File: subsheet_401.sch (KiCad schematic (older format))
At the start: 16 parts, among them U401 STE_GSTSHIFTER_PHY

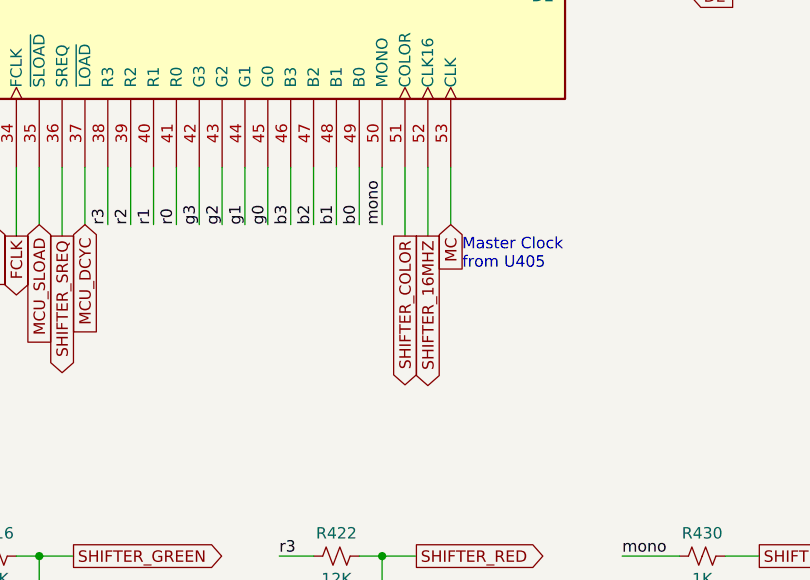
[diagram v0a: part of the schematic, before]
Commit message: Delete circuitry related to PAL/NTSC and modulator
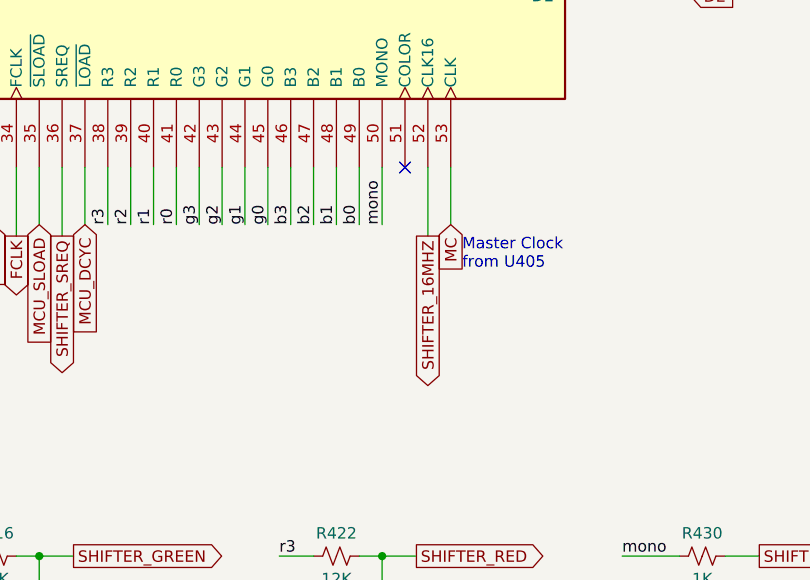
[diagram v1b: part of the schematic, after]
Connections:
- net SHIFTER_COLOR: no longer names the net of U401.51 (COLOR)
- no-connect marks 0 -> 1
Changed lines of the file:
@@
 Text GLabel 4800 2050 1    50   Input ~ 0
 MCU_RDAT
-Text GLabel 4800 6100 3    50   Output ~ 0
-SHIFTER_COLOR
 Text Label 4700 6050 1    50   ~ 0
 mono
@@
 	3300 5800 3300 6100
 Wire Wire Line
-	4800 5800 4800 6100
-Wire Wire Line
 	4900 5800 4900 6100
 $Comp
@@
 Wire Wire Line
 	3100 2050 3100 2300
+NoConn ~ 4800 5800
 $EndSCHEMATC

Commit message: Resolves #13 : assign 1206 hand-solder footprints to resistors
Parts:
- R411, R412, R414, R415, R416, R417, R418, R419, R422, R424, R426, R428, R430: footprint commons_passives_THT:Passive_THT_resistor_W2.54mm_L12.70mm -> Resistor_SMD:R_1206_3216Metric_Pad1.30x1.75mm_HandSolder
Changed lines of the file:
@@
 F 0 "R411" V 1400 7500 50  0000 C CNN
 F 1 "12K" V 1600 7500 50  0000 C CNN
-F 2 "commons_passives_THT:Passive_THT_resistor_W2.54mm_L12.70mm" H 1500 7500 50  0001 C CNN
+F 2 "Resistor_SMD:R_1206_3216Metric_Pad1.30x1.75mm_HandSolder" H 1500 7500 50  0001 C CNN
 F 3 "~" H 1500 7500 50  0001 C CNN
 	1    1500 7500
@@
 F 0 "R412" V 1400 8000 50  0000 C CNN
 F 1 "1K5" V 1600 8000 50  0000 C CNN
-F 2 "commons_passives_THT:Passive_THT_resistor_W2.54mm_L12.70mm" H 1500 8000 50  0001 C CNN
+F 2 "Resistor_SMD:R_1206_3216Metric_Pad1.30x1.75mm_HandSolder" H 1500 8000 50  0001 C CNN
 F 3 "~" H 1500 8000 50  0001 C CNN
 	1    1500 8000
@@
 F 0 "R414" V 1400 8500 50  0000 C CNN
 F 1 "3K" V 1600 8500 50  0000 C CNN
-F 2 "commons_passives_THT:Passive_THT_resistor_W2.54mm_L12.70mm" H 1500 8500 50  0001 C CNN
+F 2 "Resistor_SMD:R_1206_3216Metric_Pad1.30x1.75mm_HandSolder" H 1500 8500 50  0001 C CNN
 F 3 "~" H 1500 8500 50  0001 C CNN
 	1    1500 8500
@@
 F 0 "R415" V 1400 9000 50  0000 C CNN
 F 1 "6K2" V 1600 9000 50  0000 C CNN
-F 2 "commons_passives_THT:Passive_THT_resistor_W2.54mm_L12.70mm" H 1500 9000 50  0001 C CNN
+F 2 "Resistor_SMD:R_1206_3216Metric_Pad1.30x1.75mm_HandSolder" H 1500 9000 50  0001 C CNN
 F 3 "~" H 1500 9000 50  0001 C CNN
 	1    1500 9000
@@
 F 0 "R416" V 2900 7500 50  0000 C CNN
 F 1 "12K" V 3100 7500 50  0000 C CNN
-F 2 "commons_passives_THT:Passive_THT_resistor_W2.54mm_L12.70mm" H 3000 7500 50  0001 C CNN
+F 2 "Resistor_SMD:R_1206_3216Metric_Pad1.30x1.75mm_HandSolder" H 3000 7500 50  0001 C CNN
 F 3 "~" H 3000 7500 50  0001 C CNN
 	1    3000 7500
@@
 F 0 "R417" V 2900 8000 50  0000 C CNN
 F 1 "1K5" V 3100 8000 50  0000 C CNN
-F 2 "commons_passives_THT:Passive_THT_resistor_W2.54mm_L12.70mm" H 3000 8000 50  0001 C CNN
+F 2 "Resistor_SMD:R_1206_3216Metric_Pad1.30x1.75mm_HandSolder" H 3000 8000 50  0001 C CNN
 F 3 "~" H 3000 8000 50  0001 C CNN
 	1    3000 8000
@@
 F 0 "R418" V 2900 8500 50  0000 C CNN
 F 1 "3K" V 3100 8500 50  0000 C CNN
-F 2 "commons_passives_THT:Passive_THT_resistor_W2.54mm_L12.70mm" H 3000 8500 50  0001 C CNN
+F 2 "Resistor_SMD:R_1206_3216Metric_Pad1.30x1.75mm_HandSolder" H 3000 8500 50  0001 C CNN
 F 3 "~" H 3000 8500 50  0001 C CNN
 	1    3000 8500
@@
 F 0 "R419" V 2900 9000 50  0000 C CNN
 F 1 "6K2" V 3100 9000 50  0000 C CNN
-F 2 "commons_passives_THT:Passive_THT_resistor_W2.54mm_L12.70mm" H 3000 9000 50  0001 C CNN
+F 2 "Resistor_SMD:R_1206_3216Metric_Pad1.30x1.75mm_HandSolder" H 3000 9000 50  0001 C CNN
 F 3 "~" H 3000 9000 50  0001 C CNN
 	1    3000 9000
@@
 F 0 "R422" V 4400 7500 50  0000 C CNN
 F 1 "12K" V 4600 7500 50  0000 C CNN
-F 2 "commons_passives_THT:Passive_THT_resistor_W2.54mm_L12.70mm" H 4500 7500 50  0001 C CNN
+F 2 "Resistor_SMD:R_1206_3216Metric_Pad1.30x1.75mm_HandSolder" H 4500 7500 50  0001 C CNN
 F 3 "~" H 4500 7500 50  0001 C CNN
 	1    4500 7500
@@
 F 0 "R424" V 4400 8000 50  0000 C CNN
 F 1 "1K5" V 4600 8000 50  0000 C CNN
-F 2 "commons_passives_THT:Passive_THT_resistor_W2.54mm_L12.70mm" H 4500 8000 50  0001 C CNN
+F 2 "Resistor_SMD:R_1206_3216Metric_Pad1.30x1.75mm_HandSolder" H 4500 8000 50  0001 C CNN
 F 3 "~" H 4500 8000 50  0001 C CNN
 	1    4500 8000
@@
 F 0 "R426" V 4400 8500 50  0000 C CNN
 F 1 "3K" V 4600 8500 50  0000 C CNN
-F 2 "commons_passives_THT:Passive_THT_resistor_W2.54mm_L12.70mm" H 4500 8500 50  0001 C CNN
+F 2 "Resistor_SMD:R_1206_3216Metric_Pad1.30x1.75mm_HandSolder" H 4500 8500 50  0001 C CNN
 F 3 "~" H 4500 8500 50  0001 C CNN
 	1    4500 8500
@@
 F 0 "R428" V 4400 9000 50  0000 C CNN
 F 1 "6K2" V 4600 9000 50  0000 C CNN
-F 2 "commons_passives_THT:Passive_THT_resistor_W2.54mm_L12.70mm" H 4500 9000 50  0001 C CNN
+F 2 "Resistor_SMD:R_1206_3216Metric_Pad1.30x1.75mm_HandSolder" H 4500 9000 50  0001 C CNN
 F 3 "~" H 4500 9000 50  0001 C CNN
 	1    4500 9000
@@
 F 0 "R430" V 6000 7500 50  0000 C CNN
 F 1 "1K" V 6200 7500 50  0000 C CNN
-F 2 "commons_passives_THT:Passive_THT_resistor_W2.54mm_L12.70mm" H 6100 7500 50  0001 C CNN
+F 2 "Resistor_SMD:R_1206_3216Metric_Pad1.30x1.75mm_HandSolder" H 6100 7500 50  0001 C CNN
 F 3 "~" H 6100 7500 50  0001 C CNN
 	1    6100 7500

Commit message: Resolves #8 : Assign 1206 hand-solder footprints to non polarized capacitors
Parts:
- C412, C413: footprint commons_passives_THT:Passive_THT_capacitor_mlcc_W2.54mm_L7.62mm -> Capacitor_SMD:C_1206_3216Metric_Pad1.33x1.80mm_HandSolder
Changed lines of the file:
@@
 F 0 "C412" H 1275 5850 50  0000 L CNN
 F 1 "0.1uF" H 1275 5650 50  0000 L CNN
-F 2 "commons_passives_THT:Passive_THT_capacitor_mlcc_W2.54mm_L7.62mm" H 1288 5600 50  0001 C CNN
+F 2 "Capacitor_SMD:C_1206_3216Metric_Pad1.33x1.80mm_HandSolder" H 1288 5600 50  0001 C CNN
 F 3 "~" H 1250 5750 50  0001 C CNN
 	1    1250 5750
@@
 F 0 "C413" H 1775 5850 50  0000 L CNN
 F 1 "0.1uF" H 1775 5650 50  0000 L CNN
-F 2 "commons_passives_THT:Passive_THT_capacitor_mlcc_W2.54mm_L7.62mm" H 1788 5600 50  0001 C CNN
+F 2 "Capacitor_SMD:C_1206_3216Metric_Pad1.33x1.80mm_HandSolder" H 1788 5600 50  0001 C CNN
 F 3 "~" H 1750 5750 50  0001 C CNN
 	1    1750 5750

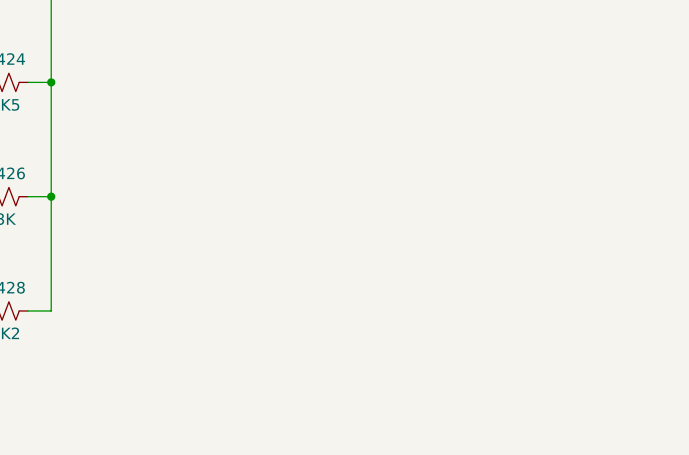
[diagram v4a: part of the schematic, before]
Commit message: Resolves #24 : Add an internal port to make easier to plug a RGB2HDMI
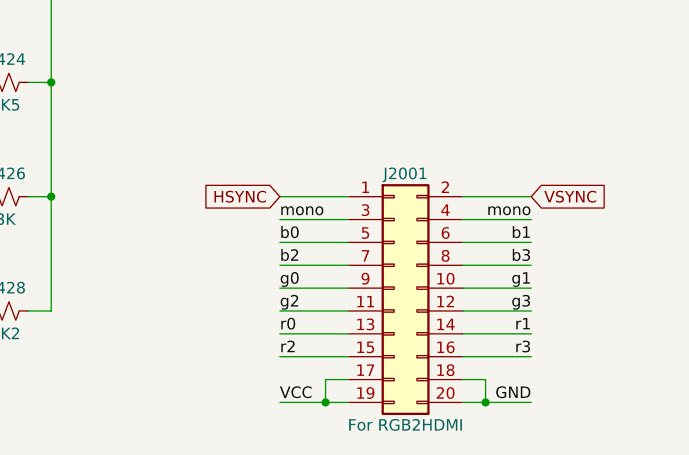
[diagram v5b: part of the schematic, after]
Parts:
- added J2001: For RGB2HDMI, Connector_PinHeader_2.54mm:PinHeader_2x10_P2.54mm_Vertical, symbol Connector_Generic:Conn_02x10_Odd_Even
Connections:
- net GND: now also J2001.18 (Pin_18), J2001.20 (Pin_20)
- net VCC: now also J2001.17 (Pin_17), J2001.19 (Pin_19)
- net b0: now also J2001.5 (Pin_5)
- net b1: now also J2001.6 (Pin_6)
- net b2: now also J2001.7 (Pin_7)
- net b3: now also J2001.8 (Pin_8)
- net g0: now also J2001.9 (Pin_9)
- net g1: now also J2001.10 (Pin_10)
- net g2: now also J2001.11 (Pin_11)
- net g3: now also J2001.12 (Pin_12)
- net mono: now also J2001.3 (Pin_3), J2001.4 (Pin_4)
- net r0: now also J2001.13 (Pin_13)
- net r1: now also J2001.14 (Pin_14)
- net r2: now also J2001.15 (Pin_15)
- net r3: now also J2001.16 (Pin_16)
- new net HSYNC: J2001.1 (Pin_1)
- new net VSYNC: J2001.2 (Pin_2)
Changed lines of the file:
@@
 	3100 2050 3100 2300
 NoConn ~ 4800 5800
+$Comp
+L Connector_Generic:Conn_02x10_Odd_Even J2001
+U 1 1 629BA30C
+P 6200 8900
+F 0 "J2001" H 6250 9400 50  0000 C CNN
+F 1 "For RGB2HDMI" H 6250 8300 50  0000 C CNN
+F 2 "Connector_PinHeader_2.54mm:PinHeader_2x10_P2.54mm_Vertical" H 6200 8900 50  0001 C CNN
+F 3 "~" H 6200 8900 50  0001 C CNN
+	1    6200 8900
+	1    0    0    -1
+$EndComp
+Text GLabel 5700 8500 0    50   Input ~ 0
+HSYNC
+Text GLabel 6800 8500 2    50   Input ~ 0
+VSYNC
+Text Label 5700 9400 0    50   ~ 0
+VCC
+Text Label 6800 9400 2    50   ~ 0
+GND
+Text Label 5700 8600 0    50   ~ 0
+mono
+Text Label 5700 8700 0    50   ~ 0
+b0
+Text Label 6800 8700 2    50   ~ 0
+b1
+Text Label 5700 8800 0    50   ~ 0
+b2
+Text Label 6800 8800 2    50   ~ 0
+b3
+Text Label 5700 8900 0    50   ~ 0
+g0
+Text Label 6800 8900 2    50   ~ 0
+g1
+Text Label 5700 9000 0    50   ~ 0
+g2
+Text Label 6800 9000 2    50   ~ 0
+g3
+Text Label 5700 9100 0    50   ~ 0
+r0
+Text Label 6800 9100 2    50   ~ 0
+r1
+Text Label 5700 9200 0    50   ~ 0
+r2
+Text Label 6800 9200 2    50   ~ 0
+r3
+Wire Wire Line
+	5700 8500 6000 8500
+Wire Wire Line
+	5700 8600 6000 8600
+Wire Wire Line
+	5700 8700 6000 8700
+Wire Wire Line
+	5700 8800 6000 8800
+Wire Wire Line
+	5700 8900 6000 8900
+Wire Wire Line
+	5700 9000 6000 9000
+Wire Wire Line
+	5700 9100 6000 9100
+Wire Wire Line
+	5700 9200 6000 9200
+Wire Wire Line
+	5700 9400 5900 9400
+Wire Wire Line
+	6500 8500 6800 8500
+Wire Wire Line
+	6500 8600 6800 8600
+Wire Wire Line
+	6500 8700 6800 8700
+Wire Wire Line
+	6500 8800 6800 8800
+Wire Wire Line
+	6500 8900 6800 8900
+Wire Wire Line
+	6500 9000 6800 9000
+Wire Wire Line
+	6500 9100 6800 9100
+Wire Wire Line
+	6500 9200 6800 9200
+Wire Wire Line
+	6500 9400 6600 9400
+Wire Wire Line
+	6000 9300 5900 9300
+Wire Wire Line
+	5900 9300 5900 9400
+Connection ~ 5900 9400
+Wire Wire Line
+	5900 9400 6000 9400
+Wire Wire Line
+	6500 9300 6600 9300
+Wire Wire Line
+	6600 9300 6600 9400
+Connection ~ 6600 9400
+Wire Wire Line
+	6600 9400 6800 9400
+Text Label 6800 8600 2    50   ~ 0
+mono
 $EndSCHEMATC
